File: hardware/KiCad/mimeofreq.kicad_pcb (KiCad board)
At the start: 2 copper layers, 60 x 60 mm, 45 parts, among them J1 AudioJack2, J2 AudioJack2, J3 Jack-DC, SW1 SW_SPST, SW2 SW_SPST, SW3 SW_SPDT, U1 MCP6022, U2 MCP6022

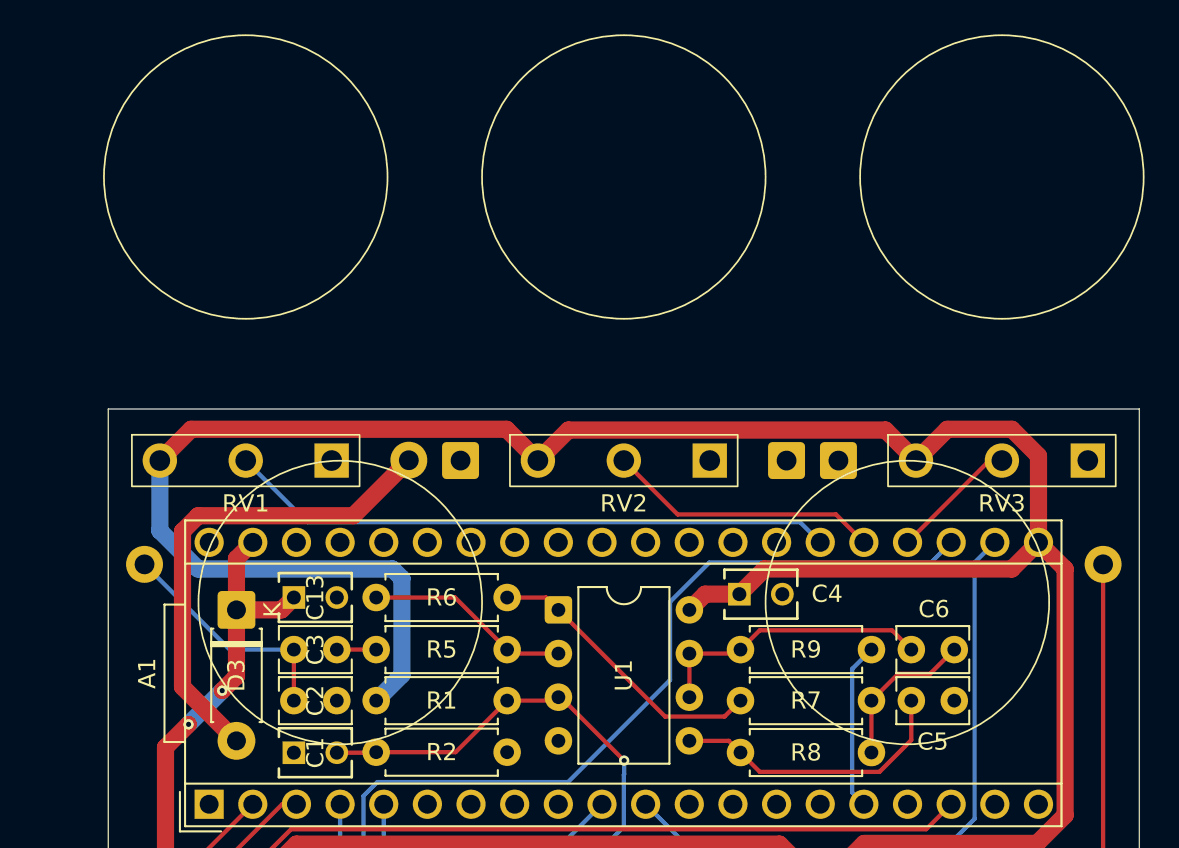
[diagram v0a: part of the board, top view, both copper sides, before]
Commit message: Silkscreen text (jacks).
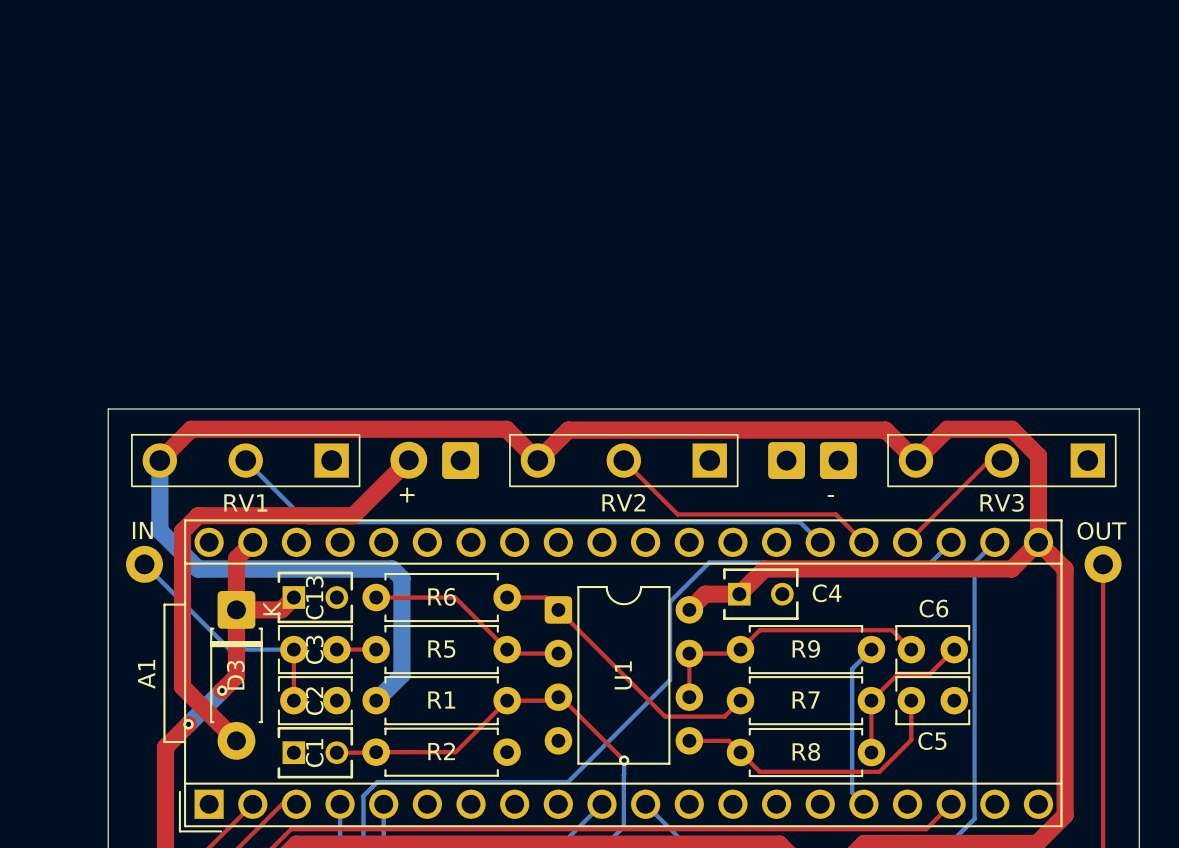
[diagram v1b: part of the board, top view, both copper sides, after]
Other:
- board text added: "+"
- board text added: "-"
- board text added: "IN"
- board text added: "OUT"
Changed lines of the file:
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@@
 		(sheetname "/")
 		(sheetfile "mimeofreq.kicad_sch")
-		(units
-			(unit
-				(name "A")
-				(pins "1" "3" "2")
-			)
-		)
 		(attr smd)
 		(duplicate_pad_numbers_are_jumpers no)
@@
 			)
 			(fill no)
-			(layer "F.SilkS")
+			(layer "B.SilkS")
 		)
 		(fp_rect
@@
 		(sheetname "/")
 		(sheetfile "mimeofreq.kicad_sch")
-		(units
-			(unit
-				(name "A")
-				(pins "1" "3" "2")
-			)
-		)
 		(attr smd)
 		(duplicate_pad_numbers_are_jumpers no)
@@
 			)
 			(fill no)
-			(layer "F.SilkS")
+			(layer "B.SilkS")
 		)
 		(fp_rect
@@
 		(sheetname "/")
 		(sheetfile "mimeofreq.kicad_sch")
-		(units
-			(unit
-				(name "A")
-				(pins "1" "3" "2")
-			)
-		)
 		(attr smd)
 		(duplicate_pad_numbers_are_jumpers no)
@@
 			)
 			(fill no)
-			(layer "F.SilkS")
+			(layer "B.SilkS")
 		)
 		(fp_rect
@@
 		(sheetname "/")
 		(sheetfile "mimeofreq.kicad_sch")
-		(units
-			(unit
-				(name "A")
-				(pins "1" "3" "2")
-			)
-		)
 		(attr smd)
 		(duplicate_pad_numbers_are_jumpers no)
@@
 			)
 			(fill no)
-			(layer "F.SilkS")
+			(layer "B.SilkS")
 		)
 		(fp_rect
@@
 		(sheetname "/")
 		(sheetfile "mimeofreq.kicad_sch")
-		(units
-			(unit
-				(name "A")
-				(pins "1" "3" "2")
-			)
-		)
 		(attr smd)
 		(duplicate_pad_numbers_are_jumpers no)
@@
 			)
 			(fill no)
-			(layer "F.SilkS")
+			(layer "B.SilkS")
 		)
 		(fp_rect
@@
 		(layer "Edge.Cuts")
 	)
+	(gr_text "IN"
+		(at 115.3 59.69 0)
+		(layer "F.SilkS")
+		(effects
+			(font
+				(size 1 1)
+				(thickness 0.15)
+			)
+			(justify left bottom)
+		)
+	)
+	(gr_text "+"
+		(at 130.82 57.56 0)
+		(layer "F.SilkS")
+		(effects
+			(font
+				(size 1 1)
+				(thickness 0.15)
+			)
+			(justify left bottom)
+		)
+	)
+	(gr_text "-"
+		(at 155.8 57.56 0)
+		(layer "F.SilkS")
+		(effects
+			(font
+				(size 1 1)
+				(thickness 0.15)
+			)
+			(justify left bottom)
+		)
+	)
+	(gr_text "OUT"
+		(at 170.325 59.72 0)
+		(layer "F.SilkS")
+		(effects
+			(font
+				(size 1 1)
+				(thickness 0.15)
+			)
+			(justify left bottom)
+		)
+	)
 	(segment

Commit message: Silkscreen text (title).
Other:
- board text added: "mimeofreq"

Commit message: Ground plane.
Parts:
- moved C13 0.15 mm to (124.8, 62.8)
- moved R6 0.15 mm to (129.6, 62.8)
- moved C5 0.09 mm to (163.2, 65.9)
- moved R5 0.09 mm to (129.6, 65.9)
- moved R9 0.09 mm to (150.8, 65.9)
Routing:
- net /POT5: track 22.1 -> 32.0 mm
- net +3V3: vias 0 -> 1
- added copper zone on B.Cu, net GND
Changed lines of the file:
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@@
 	(footprint "Capacitor_THT:C_Rect_L4.0mm_W2.5mm_P2.50mm"
 		(layer "F.Cu")
-		(at 127.3 66 180)
+		(at 127.3 65.975 180)
 		(descr "C, Rect series, Radial, pin pitch=2.50mm, length*width=4*2.5mm^2, Capacitor")
 		(tags "C Rect series Radial pin pitch 2.50mm length 4mm width 2.5mm Capacitor")
@@
 	(footprint "Resistor_THT:R_Axial_DIN0207_L6.3mm_D2.5mm_P7.62mm_Horizontal"
 		(layer "F.Cu")
-		(at 150.79 66)
+		(at 150.79 65.91)
 		(descr "Resistor, Axial_DIN0207 series, Axial, Horizontal, pin pitch=7.62mm, 0.25W = 1/4W, length*diameter=6.3*2.5mm^2, http://cdn-reichelt.de/documents/datenblatt/B400/1_4W%23YAG.pdf")
 		(tags "Resistor Axial_DIN0207 series Axial Horizontal pin pitch 7.62mm 0.25W = 1/4W length 6.3mm diameter 2.5mm")
@@
 	(footprint "Capacitor_THT_Custom:C_Rect_L4.0mm_W2.6mm_P2.50mm"
 		(layer "F.Cu")
-		(at 150.725 62.775)
+		(at 150.725 62.725)
 		(descr "C, Rect series, Radial; Designed for K104x15X7RF5xxx 0.1uF X7R ceramic capacitor.")
 		(tags "K104K15X7RF5TL2 ")
@@
 		)
 		(fp_text user "K"
-			(at 0 -2.1 90)
+			(at -1.93 0.01 90)
 			(layer "F.SilkS")
 			(effects
@@
 	(footprint "Capacitor_THT_Custom:C_Rect_L4.0mm_W2.6mm_P2.50mm"
 		(layer "F.Cu")
-		(at 124.8 72)
+		(at 124.8 72.025)
 		(descr "C, Rect series, Radial; Designed for K104x15X7RF5xxx 0.1uF X7R ceramic capacitor.")
 		(tags "K104K15X7RF5TL2 ")
@@
 	(footprint "Capacitor_THT:C_Rect_L4.0mm_W2.5mm_P2.50mm"
 		(layer "F.Cu")
-		(at 163.23 66 180)
+		(at 163.23 65.91 180)
 		(descr "C, Rect series, Radial, pin pitch=2.50mm, length*width=4*2.5mm^2, Capacitor")
 		(tags "C Rect series Radial pin pitch 2.50mm length 4mm width 2.5mm Capacitor")
@@
 	(footprint "Resistor_THT:R_Axial_DIN0207_L6.3mm_D2.5mm_P7.62mm_Horizontal"
 		(layer "F.Cu")
-		(at 129.59 62.97)
+		(at 129.59 62.82)
 		(descr "Resistor, Axial_DIN0207 series, Axial, Horizontal, pin pitch=7.62mm, 0.25W = 1/4W, length*diameter=6.3*2.5mm^2, http://cdn-reichelt.de/documents/datenblatt/B400/1_4W%23YAG.pdf")
 		(tags "Resistor Axial_DIN0207 series Axial Horizontal pin pitch 7.62mm 0.25W = 1/4W length 6.3mm diameter 2.5mm")
@@
 	(footprint "Capacitor_THT_Custom:C_Rect_L4.0mm_W2.6mm_P2.50mm"
 		(layer "F.Cu")
-		(at 124.8 62.97)
+		(at 124.8 62.82)
 		(descr "C, Rect series, Radial; Designed for K104x15X7RF5xxx 0.1uF X7R ceramic capacitor.")
 		(tags "K104K15X7RF5TL2 ")
@@
 	(footprint "Resistor_THT:R_Axial_DIN0207_L6.3mm_D2.5mm_P7.62mm_Horizontal"
 		(layer "F.Cu")
-		(at 129.59 66)
+		(at 129.59 65.91)
 		(descr "Resistor, Axial_DIN0207 series, Axial, Horizontal, pin pitch=7.62mm, 0.25W = 1/4W, length*diameter=6.3*2.5mm^2, http://cdn-reichelt.de/documents/datenblatt/B400/1_4W%23YAG.pdf")
 		(tags "Resistor Axial_DIN0207 series Axial Horizontal pin pitch 7.62mm 0.25W = 1/4W length 6.3mm diameter 2.5mm")
@@
 	)
 	(segment
+		(start 131.09 67.47)
+		(end 129.59 68.97)
+		(width 1)
+		(layer "F.Cu")
+		(net "+3V3")
+	)
+	(segment
 		(start 169.68 75.642032)
 		(end 168.042032 77.28)
@@
 	)
 	(segment
+		(start 131.09 63.71)
+		(end 131.09 67.47)
+		(width 1)
+		(layer "F.Cu")
+		(net "+3V3")
+	)
+	(segment
 		(start 157.98 77.28)
 		(end 155.5 79.76)
@@
 	)
 	(segment
+		(start 131.08 63.7)
+		(end 131.09 63.71)
+		(width 1)
+		(layer "F.Cu")
+		(net "+3V3")
+	)
+	(segment
 		(start 140.775 53.225)
 		(end 159.225 53.225)
@@
 		(net "+3V3")
 	)
+	(via
+		(at 131.08 63.7)
+		(size 0.6)
+		(drill 0.3)
+		(layers "F.Cu" "B.Cu")
+		(net "+3V3")
+	)
 	(segment
 		(start 119.227968 61.31)
@@
 	)
 	(segment
-		(start 131.09 61.86)
-		(end 131.09 67.47)
+		(start 131.09 63.69)
+		(end 131.08 63.7)
 		(width 1)
 		(layer "B.Cu")
@@
 	)
 	(segment
-		(start 117 59.082032)
-		(end 119.227968 61.31)
+		(start 131.09 61.86)
+		(end 131.09 63.69)
 		(width 1)
 		(layer "B.Cu")
@@
 	)
 	(segment
-		(start 131.09 67.47)
-		(end 129.59 68.97)
+		(start 117 59.082032)
+		(end 119.227968 61.31)
 		(width 1)
 		(layer "B.Cu")
@@
 	)
 	(segment
+		(start 129.73 91.23)
+		(end 134.35 95.85)
+		(width 0.25)
+		(layer "F.Cu")
+		(net "Net-(C9-Pad1)")
+	)
+	(segment
 		(start 140.18 95.83)
 		(end 140.18 98.86)
@@
 	)
 	(segment
-		(start 129.73 91.23)
-		(end 135.58 91.23)
+		(start 134.35 95.85)
+		(end 140.16 95.85)
 		(width 0.25)
 		(layer "F.Cu")
@@
 	)
 	(segment
-		(start 135.58 91.23)
+		(start 140.16 95.85)
 		(end 140.18 95.83)
 		(width 0.25)
@@
 	)
 	(segment
-		(start 150.56 66.23)
-		(end 150.79 66)
+		(start 152.07 64.72)
+		(end 150.56 66.23)
 		(width 0.25)
 		(layer "F.Cu")
@@
 	)
 	(segment
-		(start 159.605 64.875)
-		(end 151.915 64.875)
+		(start 159.45 64.72)
+		(end 152.07 64.72)
 		(width 0.25)
 		(layer "F.Cu")
@@
 	)
 	(segment
-		(start 151.915 64.875)
-		(end 150.79 66)
+		(start 147.815 66.23)
+		(end 147.815 68.77)
 		(width 0.25)
 		(layer "F.Cu")
@@
 	(segment
 		(start 160.73 66)
-		(end 159.605 64.875)
+		(end 159.45 64.72)
 		(width 0.25)
 		(layer "F.Cu")
@@
 	)
 	(segment
-		(start 147.815 66.23)
-		(end 147.815 68.77)
+		(start 150.47 66.23)
+		(end 150.79 65.91)
 		(width 0.25)
 		(layer "F.Cu")
@@
 	(segment
 		(start 147.815 66.23)
-		(end 150.56 66.23)
+		(end 150.47 66.23)
 		(width 0.25)
 		(layer "F.Cu")
@@
 	)
 	(segment
-		(start 137.47 66.23)
-		(end 140.195 66.23)
+		(start 129.59 62.82)
+		(end 134.12 62.82)
 		(width 0.25)
 		(layer "F.Cu")
@@
 	)
 	(segment
-		(start 134.18 62.97)
-		(end 137.21 66)
+		(start 137.47 66.23)
+		(end 140.195 66.23)
 		(width 0.25)
 		(layer "F.Cu")
@@
 	)
 	(segment
-		(start 129.59 62.97)
-		(end 134.18 62.97)
+		(start 134.12 62.82)
+		(end 137.21 65.91)
 		(width 0.25)
 		(layer "F.Cu")
@@
 	)
 	(segment
-		(start 164.415 60.935)
-		(end 165.59 59.76)
+		(start 169.69 59.58)
+		(end 169.69 75.69)
 		(width 0.25)
 		(layer "B.Cu")
@@
 	)
 	(segment
-		(start 160.5 79.76)
-		(end 164.415 75.845)
+		(start 168.695 58.585)
+		(end 169.69 59.58)
 		(width 0.25)
 		(layer "B.Cu")
@@
 	)
 	(segment
-		(start 164.415 75.845)
-		(end 164.415 60.935)
+		(start 169.69 75.69)
+		(end 168.06 77.32)
+		(width 0.25)
+		(layer "B.Cu")
+		(net "/POT5")
+	)
+	(segment
+		(start 168.06 77.32)
+		(end 162.94 77.32)
+		(width 0.25)
+		(layer "B.Cu")
+		(net "/POT5")
+	)
+	(segment
+		(start 165.59 59.76)
+		(end 166.765 58.585)
+		(width 0.25)
+		(layer "B.Cu")
+		(net "/POT5")
+	)
+	(segment
+		(start 166.765 58.585)
+		(end 168.695 58.585)
+		(width 0.25)
+		(layer "B.Cu")
+		(net "/POT5")
+	)
+	(segment
+		(start 162.94 77.32)
+		(end 160.5 79.76)
 		(width 0.25)
 		(layer "B.Cu")
@@
 		(net "/POT2")
 	)
+	(zone
+		(net "GND")
+		(layer "B.Cu")
+		(hatch edge 0.5)
+		(connect_pads
+			(clearance 0.5)
+		)
+		(min_thickness 0.25)
+		(fill yes
+			(thermal_gap 0.5)
+			(thermal_bridge_width 0.5)
+			(island_removal_mode 0)
+		)
+		(polygon
+			(pts
+				(xy 114 52) (xy 174 52) (xy 174 112) (xy 114 112)
+			)
+		)
+	)
 	(embedded_fonts no)
